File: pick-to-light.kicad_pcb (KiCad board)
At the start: 2 copper layers, 75.6 x 29.8 mm, 21 parts, among them P1 CONN_02X03, P2 CONN_02X03, Q1 BC849, Q2 BC849, SW1 SW_PUSH, SW2 SW_PUSH

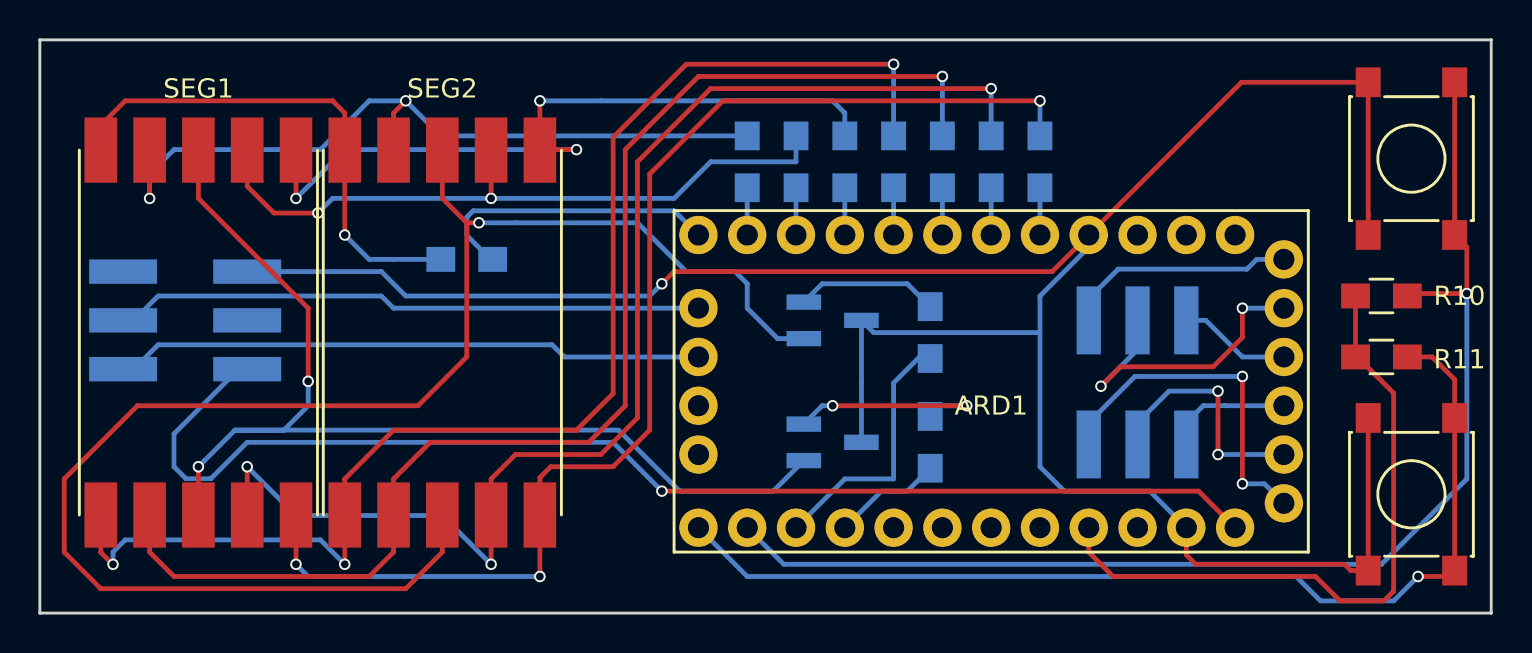
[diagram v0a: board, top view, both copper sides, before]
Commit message: Completed first itteration of layout. Needs spacing out and rerouting.
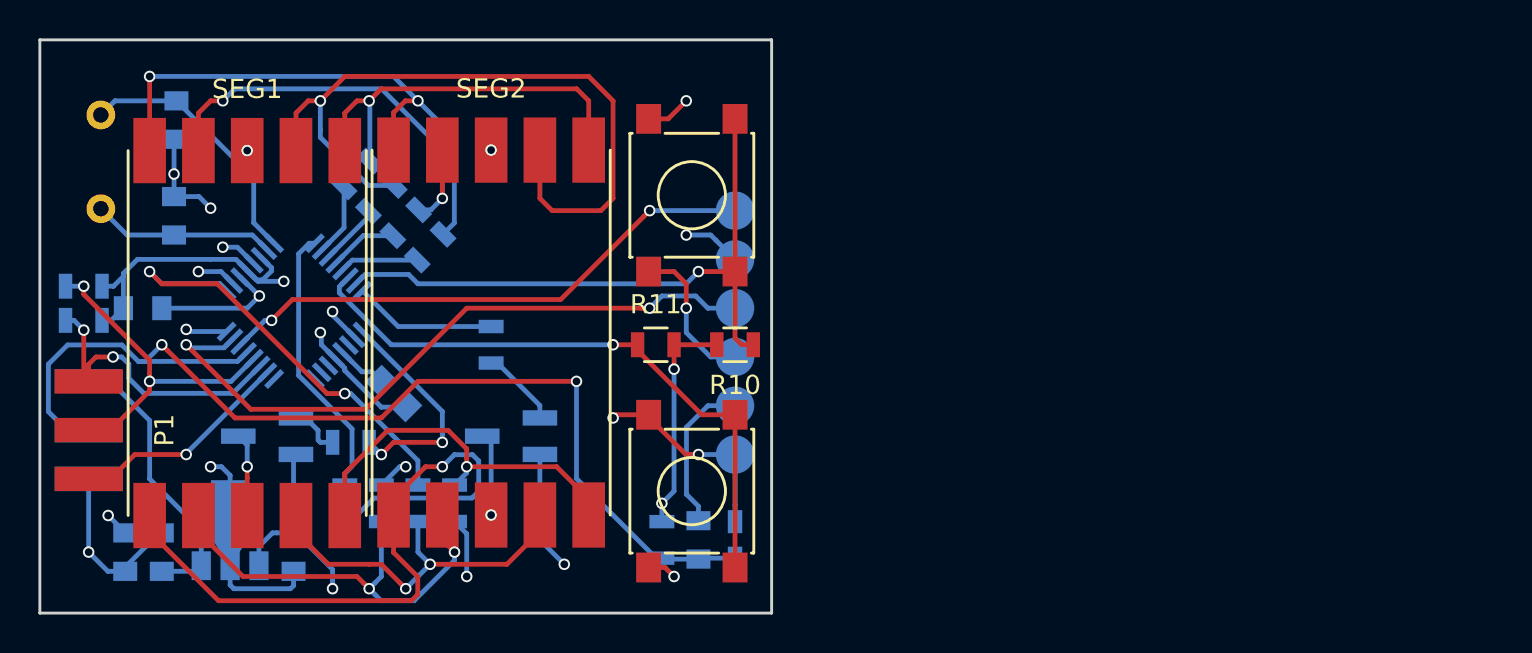
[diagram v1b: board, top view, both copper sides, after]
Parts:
- removed ARD1: Arduino_Pro_Mini_Board, PTL-footprints:ArduinoProMini
- added C1: 0.1uF, Capacitors_SMD:C_0805, B.Cu at (111.4, 99.1)
- added C2: 0.1uF, Capacitors_SMD:C_0805, B.Cu at (124.5, 103.5)
- added C3: 10uF, Capacitors_SMD:C_0805, B.Cu at (112.4, 111.8)
- added C4: 22uF, Capacitors_SMD:C_0805, B.Cu at (110.5, 111.8)
- added C5: 0.1uF, Capacitors_SMD:C_0805, B.Cu at (119.3, 111.8)
- added C6: 0.1uF, Capacitors_SMD:C_0805, B.Cu at (140.3, 111.1)
- added C7: C, Capacitors_SMD:C_0805, B.Cu at (113.0, 94.2)
- added C8: C, Capacitors_SMD:C_0805, B.Cu at (113.2, 89.3)
- added IC1: ATMEGA168PA-A, PTL-footprints:LQFP-32_5x5mm_Pitch0.5mm, B.Cu at (119.3, 99.2)
- added R13: 22k, Resistors_SMD:R_0805, B.Cu at (108.3, 99.7)
- added R14: 22k, Resistors_SMD:R_0805, B.Cu at (108.3, 97.9)
- added R15: 10k, Resistors_SMD:R_0805, B.Cu at (138.4, 111.1)
- added R16: 0, Capacitors_SMD:C_0603_HandSoldering, B.Cu at (142.2, 111.1)
- added U1: LD1117S33TR, TO_SOT_Packages_SMD:SOT89-3_Housing, B.Cu at (116.0, 110.6)
- added Y1: Crystal, Crystals:Crystal_HC49-U_Vertical, B.Cu at (109.2, 91.4)
- P1: footprint PTL-footprints:2x3-male-pin-header-smd -> PTL-footprints:2x3-male-pin-header-smd-board-edge; moved to F.Cu
- P2: footprint PTL-footprints:2x3-male-pin-header-smd -> PTL-footprints:prog_smd_pads
- R1, R2, R3, R4, R5, R6, R7, R8: value 510 -> 110; footprint Resistors_SMD:R_0805_HandSoldering -> Resistors_SMD:R_0805
- R10, R11: value 10K -> 10k; footprint Resistors_SMD:R_0805_HandSoldering -> Resistors_SMD:R_0805
- R12, R9: footprint Resistors_SMD:R_0805_HandSoldering -> Resistors_SMD:R_0805
- moved R11 37.8 mm to (138.1, 101.0), turned to 0 degrees
- moved SW2 37.5 mm to (140.0, 93.2)
- moved SW1 37.5 mm to (140.0, 108.6)
- moved R8 35.3 mm to (127.6, 109.2)
- moved R7 34.7 mm to (125.7, 109.2), turned to 90 degrees
- moved R6 34.2 mm to (123.8, 109.2), turned to 90 degrees
- moved R10 33.8 mm to (142.2, 101.0)
- moved R5 33.7 mm to (121.9, 109.2), turned to 90 degrees
- moved R9 30.2 mm to (122.2, 106.0), turned to 0 degrees
- moved Q1 29.4 mm to (117.9, 105.7), turned to 270 degrees
- moved R4 25.4 mm to (122.6, 92.1), turned to 225 degrees
- moved R12 22.9 mm to (129.5, 101.0), turned to 90 degrees
- moved R3 21.7 mm to (123.8, 93.3), turned to 225 degrees
- moved P2 21.1 mm to (142.2, 100.3), turned to 90 degrees
- moved R2 18.1 mm to (125.1, 94.6), turned to 225 degrees
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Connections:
- P1 pad 1: Net-(ARD1-Pad19) -> A4
- P1 pad 2: Net-(ARD1-Pad25) -> RAW
- P1 pad 3: Net-(ARD1-Pad18) -> A5
- P1 pad 4: Net-(P1-Pad4) -> RESET
- P1 pad 5: Net-(P1-Pad5) -> A3
- P2 pad 1: Net-(ARD1-Pad31) -> GND
- P2 pad 3: Net-(ARD1-Pad30) -> GND
- P2 pad 4: Net-(ARD1-Pad27) -> TX0
- P2 pad 5: Net-(ARD1-Pad29) -> VCC
- P2 pad 6: Net-(ARD1-Pad28) -> RX1
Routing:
- net Net-(ARD1-Pad25): track 64.6 -> 0.00 mm, vias 1 -> 0
- net RESET: track 0.00 -> 56.9 mm, vias 0 -> 2
- net Net-(Q2-Pad3): track 75.3 -> 23.4 mm, vias 1 -> 2
- net GND: track 120.8 -> 69.5 mm, vias 1 -> 13
- net Net-(R7-Pad1): track 67.1 -> 19.4 mm, vias 3 -> 2
- net Net-(R6-Pad1): track 68.9 -> 22.9 mm, vias 1 -> 2
- net Net-(R8-Pad1): track 65.1 -> 19.9 mm, vias 3 -> 1
- net TX0: track 0.00 -> 35.4 mm, vias 0 -> 2
- net Net-(R5-Pad1): track 71.1 -> 36.7 mm, vias 3 -> 1
- net Net-(IC1-Pad15): track 64.2 -> 32.9 mm
- net Net-(ARD1-Pad18): track 30.2 -> 0.00 mm
- net Net-(ARD1-Pad19): track 30.2 -> 0.00 mm
- net RX1: track 0.00 -> 28.7 mm, vias 0 -> 2
- net Net-(Q1-Pad3): track 48.4 -> 21.3 mm
- net Net-(IC1-Pad32): track 2.46 -> 25.7 mm, vias 0 -> 2
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- added copper zone on Ground.plane, net GND
- added copper zone on Power.plane, net VCC
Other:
- board size 75.6 x 29.8 mm -> 38.1 x 29.8 mm
- copper layers 2 -> 4

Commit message: Finished second round of layout.
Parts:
- removed C1: 0.1uF, Capacitors_SMD:C_0805
- C6: footprint Capacitors_SMD:C_0805 -> Capacitors_SMD:C_0805_HandSoldering
- Q1, Q2: footprint TO_SOT_Packages_SMD:SOT-23_Handsoldering -> TO_SOT_Packages_SMD:SOT-23
- R10, R11: moved to B.Cu
- moved C4 22.9 mm to (133.3, 111.8), turned to 0 degrees
- moved C3 21.0 mm to (133.3, 109.9), turned to 180 degrees
- moved R10 17.5 mm to (129.5, 88.9), turned to 90 degrees
- moved U1 16.8 mm to (132.2, 106.3), turned to 270 degrees
- moved C5 16.6 mm to (133.3, 103.0), turned to 180 degrees
- moved R11 16.4 mm to (127.0, 88.9), turned to 90 degrees
- moved Q2 9.93 mm to (131.9, 95.9)
- moved R5 8.64 mm to (113.7, 106.7)
- moved C2 8.28 mm to (131.4, 99.1), turned to 0 degrees
- moved R6 8.03 mm to (116.2, 106.7)
- moved R12 7.63 mm to (129.9, 93.3), turned to 180 degrees
- moved R7 7.43 mm to (118.7, 106.7)
- moved R1 7.24 mm to (124.5, 88.9), turned to 270 degrees
- moved R8 6.84 mm to (121.3, 106.7)
- moved R4 6.54 mm to (116.8, 88.9), turned to 270 degrees
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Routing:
- net RAW: track 14.9 -> 37.3 mm, vias 0 -> 2
- net Net-(IC1-Pad32): track 25.7 -> 7.00 mm, vias 2 -> 0
- net Net-(IC1-Pad1): track 23.7 -> 6.00 mm, vias 2 -> 0
- net GND: track 69.5 -> 52.2 mm
- net Net-(IC1-Pad14): track 32.4 -> 48.3 mm
- net Net-(IC1-Pad2): track 20.2 -> 7.39 mm, vias 2 -> 0
- net Net-(R3-Pad1): track 38.5 -> 25.7 mm, vias 1 -> 2
- net Net-(R5-Pad1): track 36.7 -> 25.2 mm, vias 1 -> 2
- net A5: track 17.8 -> 28.8 mm
- net Net-(Q1-Pad3): track 21.3 -> 31.8 mm
- net Net-(R4-Pad1): track 21.2 -> 31.4 mm, vias 1 -> 3
- net Net-(C6-Pad2): track 8.12 -> 16.8 mm
- net TX0: track 35.4 -> 26.8 mm
- net Net-(R1-Pad1): track 29.8 -> 21.3 mm, vias 2 -> 1
- net A4: track 15.7 -> 24.1 mm
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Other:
- outline, holes or cut-outs redrawn
- rule trace_min: 0.2 -> 0.007874
- rule via_min_size: 0.4 -> 0.015748

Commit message: 3d models updated, schematic pdf updated.
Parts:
- moved SW1 0.78 mm to (139.9, 109.0)
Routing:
- net Net-(IC1-Pad14): track 48.3 -> 46.0 mm
- net Net-(Q1-Pad3): track 31.8 -> 32.4 mm
